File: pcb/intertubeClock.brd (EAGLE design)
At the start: 166.3 x 37.8 mm, 77 parts, among them Q1 BSA223SP, Q10 BSA223SP, Q11 BSA223SP, Q12 BSA223SP, Q13 BSA223SP, Q14 BSA223SP, Q15 BSA223SP, Q16 BSA223SP, Q2 BSA223SP, Q3 BSA223SP, Q4 BSA223SP, Q5 BSA223SP, Q6 BSA223SP, Q7 BSA223SP, Q8 BSA223SP, Q9 BSA223SP, U1 HV5122PG, U2 HV5122PG

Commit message: -Added power supply items. -Fixed anode nets. -Adjusted resistor packages.
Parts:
- added D1, D2, D3, D4: GF1, diode:SMA-DO214AC
- added R46, R48, R50, R52: 25K, rcl:R1206
- added R47, R49, R51, R53: 50K, rcl:R2010
- R1: value 37.4K -> 150K
- R14, R15, R16, R17, R18, R19, R20, R21: device rcl:R2512 -> rcl:R1206
- R2: value 12K -> 50K
- moved JP10 35.3 mm to (34.3, 33.0), turned to 0 degrees
- moved R5 30.7 mm to (8.89, 14.0), turned to 0 degrees
- moved R2 27.9 mm to (8.89, 3.81), turned to 0 degrees
- moved R4 22.2 mm to (8.89, 24.1), turned to 0 degrees
- moved R1 21.3 mm to (8.89, 8.89), turned to 0 degrees
- moved R3 19.4 mm to (8.89, 19.1), turned to 0 degrees
- moved JP2 5.24 mm to (7.62, 33.0), turned to 0 degrees
- flipped R14 to the top
- flipped R15 to the bottom, turned to 0 degrees
- flipped R16 to the top, turned to 180 degrees
- flipped R17 to the bottom
- turned U1 to 90 degrees
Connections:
- new net HV_ENABLE: U2.15
- new net N$17: Q1.2, R47.1
- new net N$18: D1.K, R46.2
- new net N$19: Q2.2, R49.1
- new net N$20: D2.K, R48.2
- new net N$21: Q3.2, R51.1
- new net N$22: D3.K, R50.2
- new net N$24: Q4.2, R53.1
- new net N$25: D4.K, R52.2
- net A1_DIG1: now also R46.1, R47.2; no longer Q1.2
- net A1_DIG2: now also R50.1, R51.2; no longer Q3.2
- net A1_SEL#_DIG1: now also U1.35
- net A1_SEL#_DIG2: now also U1.42
- net A1_SEL#_DIG3: now also U1.5
- net A1_SEL#_DIG4: now also U1.12
- net A1_SEL#_DIG5: now also U1.19
- net A1_SEL#_DIG6: now also U2.38
- net A1_SEL#_DIG7: now also U2.1
- net A1_SEL#_DIG8: now also U2.8
- net A2_DIG1: now also R48.1, R49.2; no longer Q2.2
- net A2_DIG2: now also R52.1, R53.2; no longer Q4.2
- net A2_SEL#_DIG1: now also U1.36
- net A2_SEL#_DIG2: now also U1.43
- net A2_SEL#_DIG3: now also U1.6
- net A2_SEL#_DIG4: now also U1.13
- net A2_SEL#_DIG5: now also U1.20
- net A2_SEL#_DIG6: now also U2.39
- net A2_SEL#_DIG7: now also U2.2
- net A2_SEL#_DIG8: now also U2.9
- net HV_VBA_OFF: now also D1.A, D2.A, D3.A, D4.A
- net K01_DIG1: now also U1.37
- net K01_DIG2: now also U1.44
- net K01_DIG3: now also U1.7
- net K01_DIG4: now also U1.14
- net K01_DIG5: now also U1.21
- net K01_DIG6: now also U2.40
- net K01_DIG7: now also U2.3
- net K01_DIG8: now also U2.10
- net K23_DIG1: now also U1.38
- net K23_DIG2: now also U1.1
- net K23_DIG3: now also U1.8
- net K23_DIG4: now also U1.15
- net K23_DIG5: now also U1.22
- net K23_DIG6: now also U2.41
- net K23_DIG7: now also U2.4
- net K23_DIG8: now also U2.11
- net K45_DIG1: now also U1.39
- net K45_DIG2: now also U1.2
- net K45_DIG3: now also U1.9
- net K45_DIG4: now also U1.16
- net K45_DIG5: now also U2.35
- net K45_DIG6: now also U2.42
- net K45_DIG7: now also U2.5
- net K45_DIG8: now also U2.12
- net K67_DIG1: now also U1.40
- net K67_DIG2: now also U1.3
- net K67_DIG3: now also U1.10
- net K67_DIG4: now also U1.17
- net K67_DIG5: now also U2.36
- net K67_DIG6: now also U2.43
- net K67_DIG7: now also U2.6
- net K67_DIG8: now also U2.13
- net K89_DIG1: now also U1.41
- net K89_DIG2: now also U1.4
- net K89_DIG3: now also U1.11
- net K89_DIG4: now also U1.18
- net K89_DIG5: now also U2.37
- net K89_DIG6: now also U2.44
- net K89_DIG7: now also U2.7
- net K89_DIG8: now also U2.14
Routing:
- net K23_DIG1: track 0.00 -> 34.0 mm
- net K01_DIG1: track 0.00 -> 32.2 mm
- net K67_DIG1: track 0.00 -> 31.4 mm
- net A1_SEL#_DIG1: track 0.00 -> 30.4 mm, vias 0 -> 1
- net K45_DIG1: track 0.00 -> 29.6 mm
- net K89_DIG1: track 0.00 -> 27.7 mm
- net A2_SEL#_DIG1: track 0.00 -> 27.3 mm, vias 0 -> 1
- net N$2: track 0.00 -> 15.8 mm, vias 0 -> 2
- net S_DIG1: track 0.00 -> 8.78 mm
- net HV_VBA: track 0.00 -> 6.95 mm
- net N$1: track 0.00 -> 6.69 mm, vias 0 -> 2
- net A2_DIG1: track 0.00 -> 5.32 mm
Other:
- board text added: ">drawing_name"
- board text added: "Rev A"
- board text added: "www.andersknelson.com"

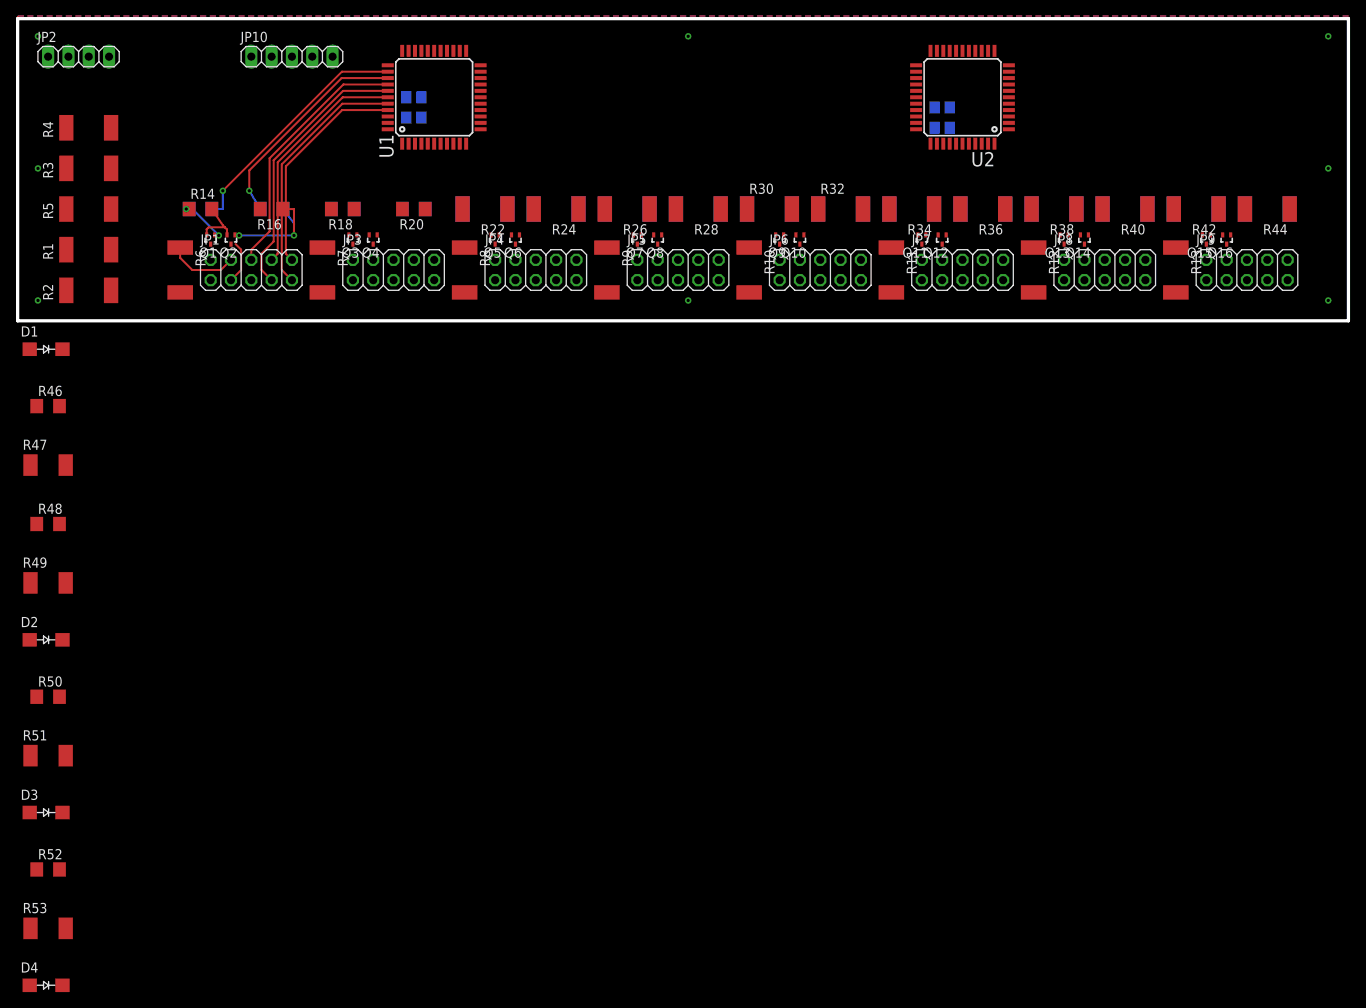
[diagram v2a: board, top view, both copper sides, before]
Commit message: -Added remaining components.
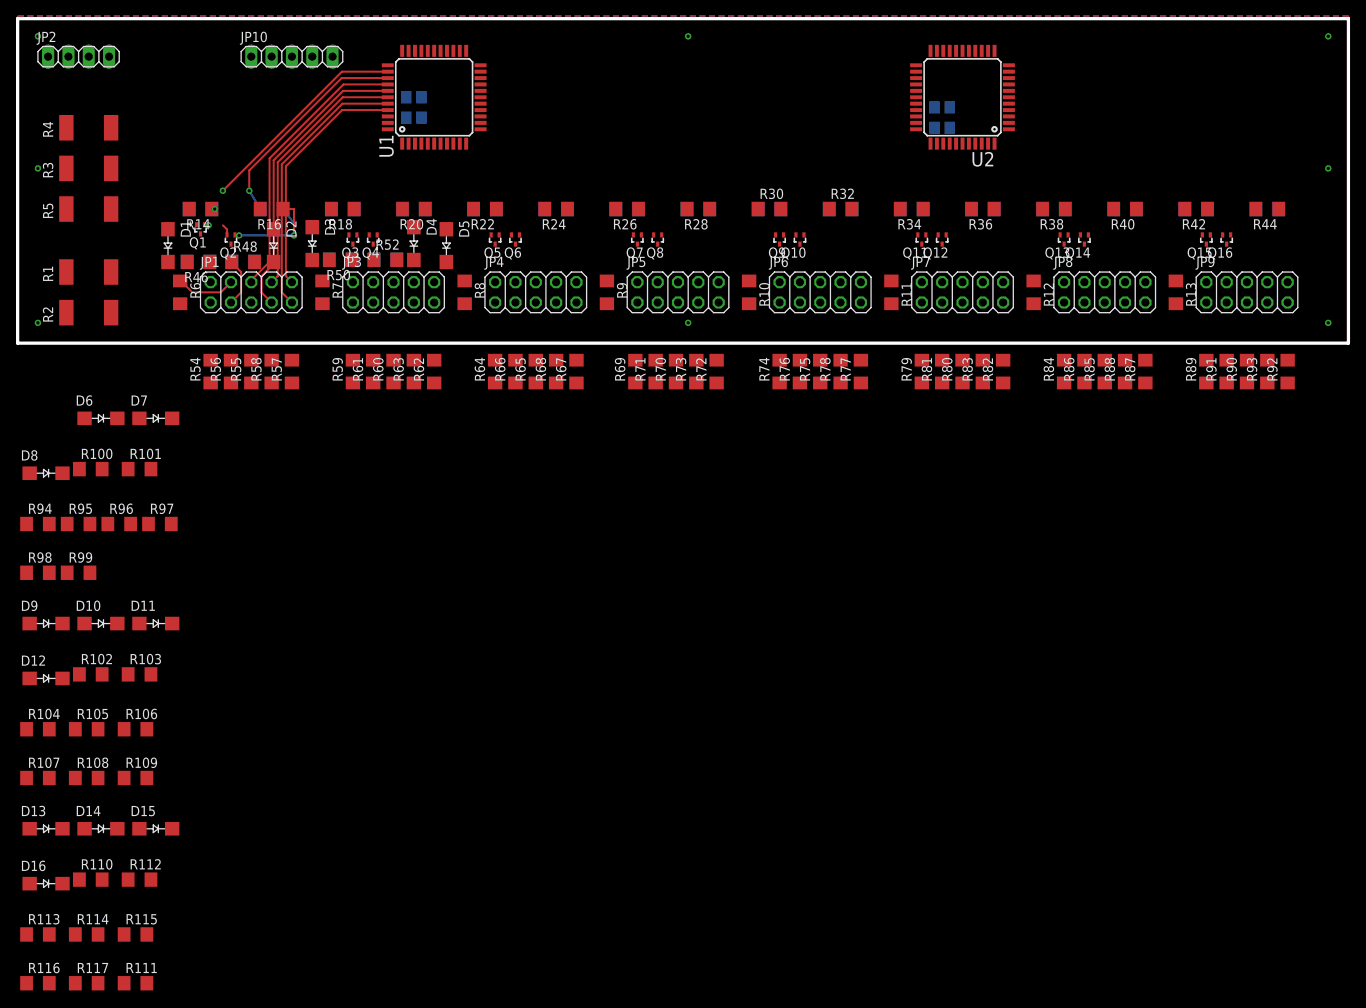
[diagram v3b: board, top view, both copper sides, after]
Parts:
- added D10, D11, D12, D13, D14, D15, D16, D5, D6, D7, D8, D9: GF1, diode:SMA-DO214AC
- added R100, R102, R104, R106, R108, R110, R112, R114, R116, R94, R96, R98: 25K, rcl:R1206
- added R101, R103, R105, R107, R109, R111, R113, R115, R117, R95, R97, R99: 15K, rcl:R1206
- added R54, R55, R56, R57, R58, R59, R60, R61, R62, R63, R64, R65, R66, R67, R68, R69, R70, R71, R72, R73, R74, R75, R76, R77, R78, R79, R80, R81, R82, R83, R84, R85, R86, R87, R88, R89, R90, R91, R92, R93: 100K, rcl:R1206
- R10, R11, R12, R13, R22, R23, R24, R25, R26, R27, R28, R29, R30, R31, R32, R33, R34, R35, R36, R37, R38, R39, R40, R41, R42, R43, R44, R45, R6, R7, R8, R9: device rcl:R2512 -> rcl:R1206
- R47, R49, R51, R53: value 50K -> 15K; device rcl:R2010 -> rcl:R1206
- moved D4 103.5 mm to (49.5, 9.65), turned to 270 degrees
- moved R53 93.6 mm to (46.0, 7.62), flipped to the bottom
- moved R52 87.1 mm to (46.0, 7.62)
- moved D3 78.5 mm to (36.8, 9.65), turned to 270 degrees
- moved R51 72.0 mm to (40.4, 7.62), flipped to the bottom, turned to 180 degrees
- moved R50 65.7 mm to (40.4, 7.62), turned to 180 degrees
- moved D2 56.9 mm to (32.0, 9.40), turned to 270 degrees
- moved R49 47.0 mm to (28.2, 7.37), flipped to the bottom
- moved R48 40.8 mm to (28.2, 7.37)
- moved R47 31.6 mm to (22.6, 7.37), flipped to the bottom, turned to 180 degrees
- moved R46 26.0 mm to (22.6, 7.37), turned to 180 degrees
- moved D1 20.0 mm to (18.8, 9.40), turned to 270 degrees
- moved R1 2.79 mm to (8.89, 6.10)
- moved R2 2.79 mm to (8.89, 1.02)
- moved JP1 2.79 mm to (29.2, 3.56)
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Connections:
- new net N$26: D5.K, R94.2
- new net N$27: D6.K, R96.2
- new net N$28: D7.K, R98.2
- new net N$29: D8.K, R100.2
- new net N$30: Q9.2, R103.1
- new net N$31: D9.K, R102.2
- new net N$32: D10.K, R104.2
- new net N$33: D11.K, R106.2
- new net N$34: D12.K, R108.2
- new net N$35: Q13.2, R111.1
- new net N$36: D13.K, R110.2
- new net N$37: D14.K, R112.2
- new net N$38: D15.K, R114.2
- new net N$39: D16.K, R116.2
- new net N$41: Q5.2, R95.1
- new net N$42: Q6.2, R97.1
- new net N$43: Q7.2, R99.1
- new net N$44: Q8.2, R101.1
- new net N$45: Q10.2, R105.1
- new net N$46: Q11.2, R107.1
- new net N$47: Q12.2, R109.1
- new net N$48: Q14.2, R113.1
- new net N$49: Q15.2, R115.1
- new net N$50: Q16.2, R117.1
- net A1_DIG3: now also R94.1, R95.2; no longer Q5.2
- net A1_DIG4: now also R98.1, R99.2; no longer Q7.2
- net A1_DIG5: now also R102.1, R103.2; no longer Q9.2
- net A1_DIG6: now also R106.1, R107.2; no longer Q11.2
- net A1_DIG7: now also R110.1, R111.2; no longer Q13.2
- net A1_DIG8: now also R114.1, R115.2; no longer Q15.2
- net A2_DIG3: now also R96.1, R97.2; no longer Q6.2
- net A2_DIG4: now also R100.1, R101.2; no longer Q8.2
- net A2_DIG5: now also R104.1, R105.2; no longer Q10.2
- net A2_DIG6: now also R108.1, R109.2; no longer Q12.2
- net A2_DIG7: now also R112.1, R113.2; no longer Q14.2
- net A2_DIG8: now also R116.1, R117.2; no longer Q16.2
- net HV_VBA_OFF: now also D10.A, D11.A, D12.A, D13.A, D14.A, D15.A, D16.A, D5.A, D6.A, D7.A, D8.A, D9.A
- net HV_VS: now also R54.1, R55.1, R56.1, R57.1, R58.1, R59.1, R60.1, R61.1, R62.1, R63.1, R64.1, R65.1, R66.1, R67.1, R68.1, R69.1, R70.1, R71.1, R72.1, R73.1, R74.1, R75.1, R76.1, R77.1, R78.1, R79.1, R80.1, R81.1, R82.1, R83.1, R84.1, R85.1, R86.1, R87.1, R88.1, R89.1, R90.1, R91.1, R92.1, R93.1
- net K01_DIG1: now also R54.2
- net K01_DIG2: now also R59.2
- net K01_DIG3: now also R64.2
- net K01_DIG4: now also R69.2
- net K01_DIG5: now also R74.2
- net K01_DIG6: now also R79.2
- net K01_DIG7: now also R84.2
- net K01_DIG8: now also R89.2
- net K23_DIG1: now also R55.2
- net K23_DIG2: now also R60.2
- net K23_DIG3: now also R65.2
- net K23_DIG4: now also R70.2
- net K23_DIG5: now also R75.2
- net K23_DIG6: now also R80.2
- net K23_DIG7: now also R85.2
- net K23_DIG8: now also R90.2
- net K45_DIG1: now also R56.2
- net K45_DIG2: now also R61.2
- net K45_DIG3: now also R66.2
- net K45_DIG4: now also R71.2
- net K45_DIG5: now also R76.2
- net K45_DIG6: now also R81.2
- net K45_DIG7: now also R86.2
- net K45_DIG8: now also R91.2
- net K67_DIG1: now also R57.2
- net K67_DIG2: now also R62.2
- net K67_DIG3: now also R67.2
- net K67_DIG4: now also R72.2
- net K67_DIG5: now also R77.2
- net K67_DIG6: now also R82.2
- net K67_DIG7: now also R87.2
- net K67_DIG8: now also R92.2
- net K89_DIG1: now also R58.2
- net K89_DIG2: now also R63.2
- net K89_DIG3: now also R68.2
- net K89_DIG4: now also R73.2
- net K89_DIG5: now also R78.2
- net K89_DIG6: now also R83.2
- net K89_DIG7: now also R88.2
- net K89_DIG8: now also R93.2
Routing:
- net HV_VBA: track 6.95 -> 1.41 mm
- net N$1: track 6.69 -> 2.02 mm
- net A1_SEL#_DIG1: track 30.4 -> 26.8 mm
- net K23_DIG1: track 34.0 -> 36.8 mm
- net K67_DIG1: track 31.4 -> 34.2 mm
- net K45_DIG1: track 29.6 -> 32.4 mm
- net K89_DIG1: track 27.7 -> 30.5 mm
- net K01_DIG1: track 32.2 -> 35.0 mm
- net S_DIG1: track 8.78 -> 7.61 mm
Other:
- board size 166.3 x 37.8 mm -> 166.3 x 40.6 mm

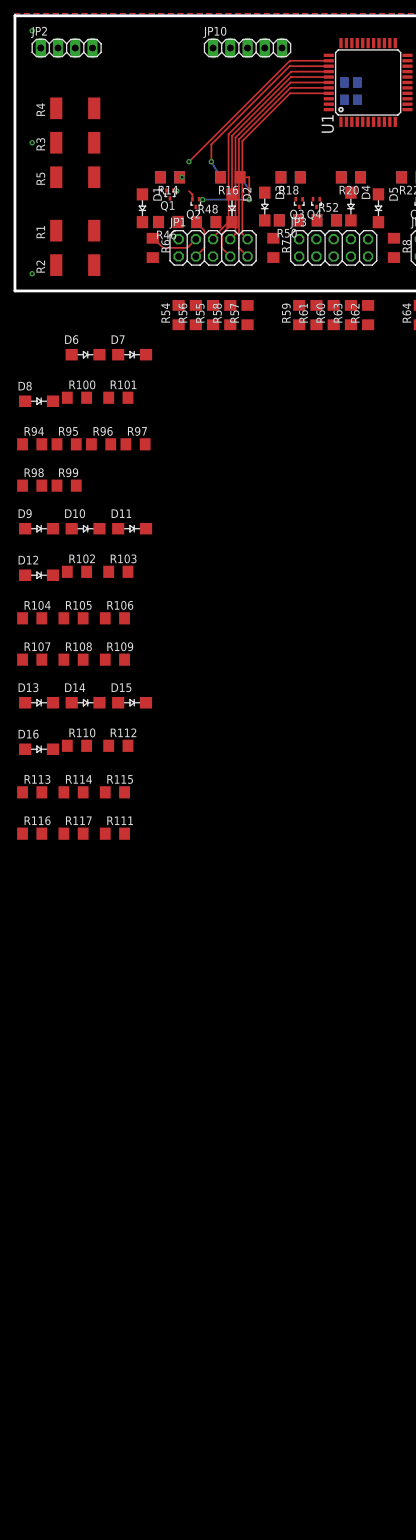
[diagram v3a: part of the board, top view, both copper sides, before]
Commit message: -ADDED LEVEL SHIFTER -BEGAN REPLACING DIODES
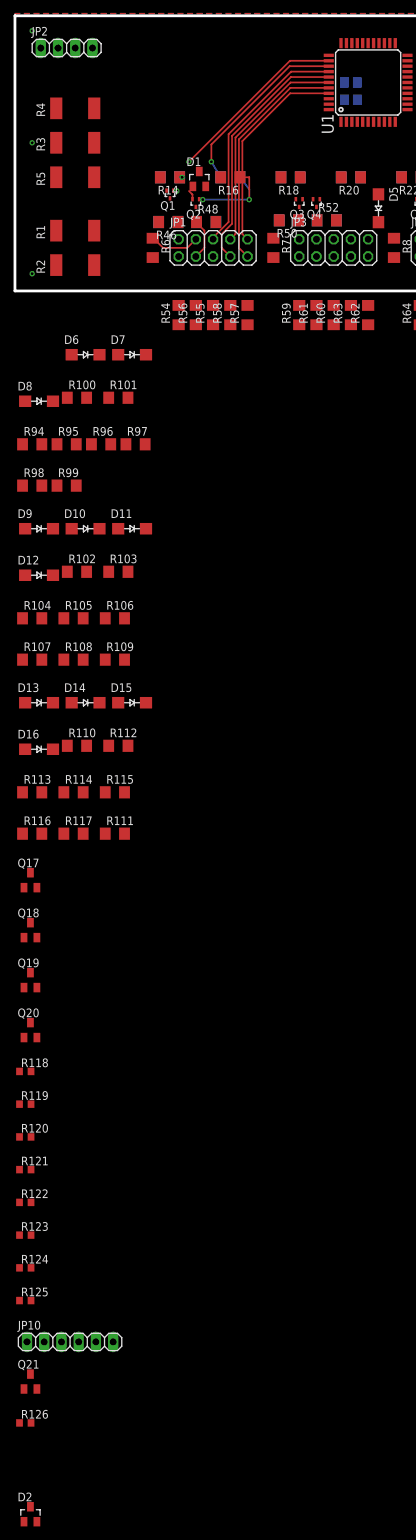
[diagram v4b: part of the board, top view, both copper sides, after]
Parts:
- removed D3, D4: GF1, diode:SMA-DO214AC
- added Q17, Q18, Q19, Q20, Q21: BSS123, transistor-small-signal:SOT23
- added R118, R119, R120, R121, R122, R123, R124, R125, R126: 10K, rcl:R0603
- D1, D2: value GF1 -> BAS40-06; device diode:SMA-DO214AC -> diode:SOT23
- JP10: device pinhead:1X05 -> pinhead:1X06
- moved D2 194.8 mm to (2.29, -183.1), turned to 0 degrees
- moved JP10 192.5 mm to (8.13, -157.7)
- moved D1 9.43 mm to (27.2, 13.7), turned to 0 degrees
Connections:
- net DATA_OUT1 renamed DATA_OUT1_HV
- new net CLK_HV: Q18.3, R123.2, U1.29
- new net DATA_IN_HV: Q17.3, R122.2, U1.33
- new net DATA_OUT: Q21.3, R126.2
- new net DATA_OUT2_HV: Q21.1, U2.23
- new net OE_HV: Q19.3, R124.2, U1.28
- new net STR_HV: Q20.3, R125.2, U1.32
- new net VCC: C1.1, C2.1, C3.1, C4.1, R122.1, R123.1, R124.1, R125.1, U1.31, U2.31
- net CLK: now also Q18.1, R119.2; no longer U1.29
- net DATA_IN: now also Q17.1, R118.2; no longer U1.33
- net GND: now also Q17.2, Q18.2, Q19.2, Q20.2, Q21.2, R118.1, R119.1, R120.1, R121.1
- net HV_VBA_OFF: now also D1.3, D2.3; no longer D1.A, D2.A, D3.A, D4.A
- net N$18: now also D1.1; no longer D1.K
- net N$20: now also D1.2; no longer D2.K
- net N$22: now also D2.1; no longer D3.K
- net N$25: now also D2.2; no longer D4.K
- net OE: now also Q19.1, R120.2; no longer U1.28
- net STR: now also Q20.1, R121.2; no longer U1.32
- net VDD: now also JP10.6, R126.1; no longer C1.1, C2.1, C3.1, C4.1, U1.31, U2.31

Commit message: -PLACED NEW COMPONENTS.
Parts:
- removed D10, D11, D12, D13, D14, D15, D16, D9: GF1, diode:SMA-DO214AC
- added D3, D4: BAS40-06, diode:SOT23
- D5, D6, D7, D8: value GF1 -> BAS40-06; device diode:SMA-DO214AC -> diode:SOT23
- moved R126 214.2 mm to (38.1, 41.4), turned to 270 degrees
- moved Q21 207.6 mm to (35.1, 41.4), turned to 270 degrees
- moved JP10 207.1 mm to (26.7, 48.5), turned to 270 degrees
- moved D2 201.2 mm to (45.0, 13.5)
- moved R125 199.7 mm to (38.1, 44.7), turned to 270 degrees
- moved R124 198.2 mm to (38.1, 48.0), turned to 270 degrees
- moved R123 196.7 mm to (38.1, 51.3), turned to 270 degrees
- moved R122 195.2 mm to (38.1, 54.6), turned to 270 degrees
- moved R121 179.6 mm to (31.8, 44.7), turned to 90 degrees
- moved R120 178.1 mm to (31.8, 48.0), turned to 90 degrees
- moved R119 176.6 mm to (31.8, 51.3), turned to 90 degrees
- moved R118 175.1 mm to (31.8, 54.6), turned to 90 degrees
- moved R116 174.4 mm to (151.6, 7.62)
- moved R117 169.2 mm to (151.6, 7.62), flipped to the bottom
- moved R114 160.9 mm to (145.8, 7.37)
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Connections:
- net HV_VBA_OFF: now also D3.3, D4.3, D5.3, D6.3, D7.3, D8.3; no longer D10.A, D11.A, D12.A, D13.A, D14.A, D15.A, D16.A, D5.A, D6.A, D7.A, D8.A, D9.A
- net N$26: now also D3.1; no longer D5.K
- net N$27: now also D3.2; no longer D6.K
- net N$28: now also D4.1; no longer D7.K
- net N$29: now also D4.2; no longer D8.K
- net N$31: now also D5.1; no longer D9.K
- net N$32: now also D5.2; no longer D10.K
- net N$33: now also D6.1; no longer D11.K
- net N$34: now also D6.2; no longer D12.K
- net N$36: now also D7.1; no longer D13.K
- net N$37: now also D7.2; no longer D14.K
- net N$38: now also D8.1; no longer D15.K
- net N$39: now also D8.2; no longer D16.K
